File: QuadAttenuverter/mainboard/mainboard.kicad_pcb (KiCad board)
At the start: 2 copper layers, 35.6 x 108 mm, 48 parts, among them J1 Conn_01x09, J2 Conn_02x10_Counter_Clockwise, J3 Conn_02x05_Odd_Even, U1 LM324, U2 LM324, U3 LM324, U4 LM324, U5 LM324

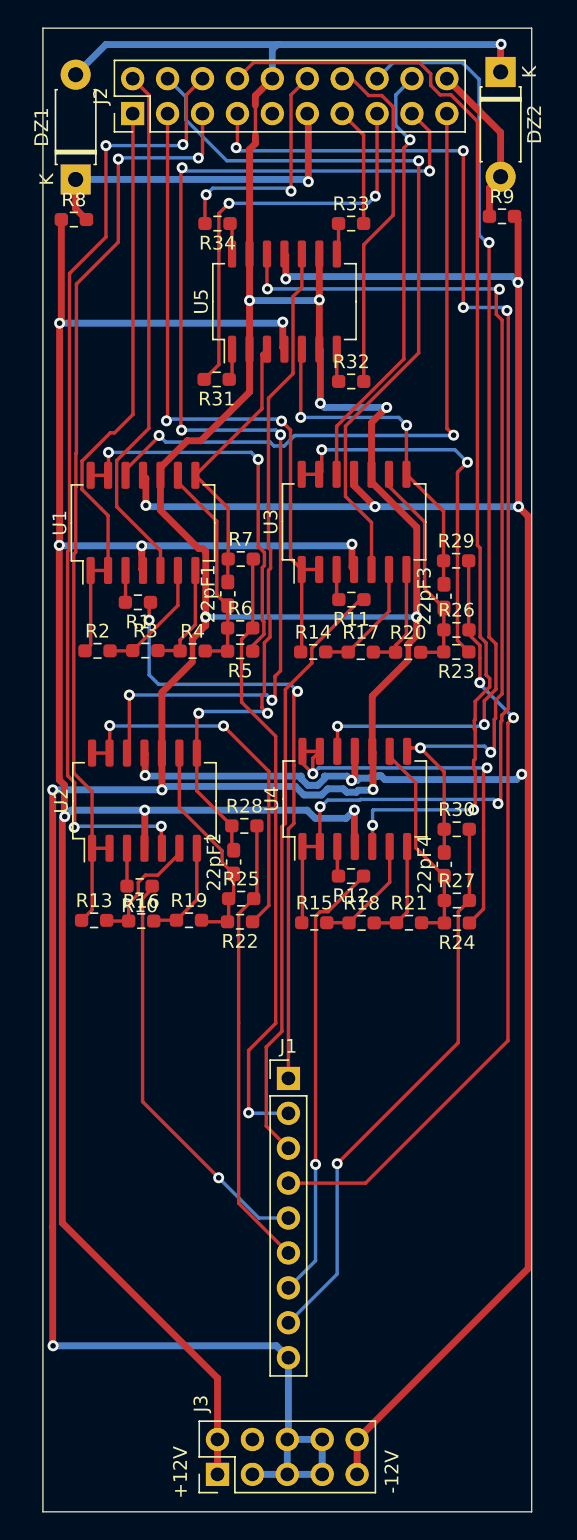
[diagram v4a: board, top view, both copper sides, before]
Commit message: Add IOBoard with the right knob distance
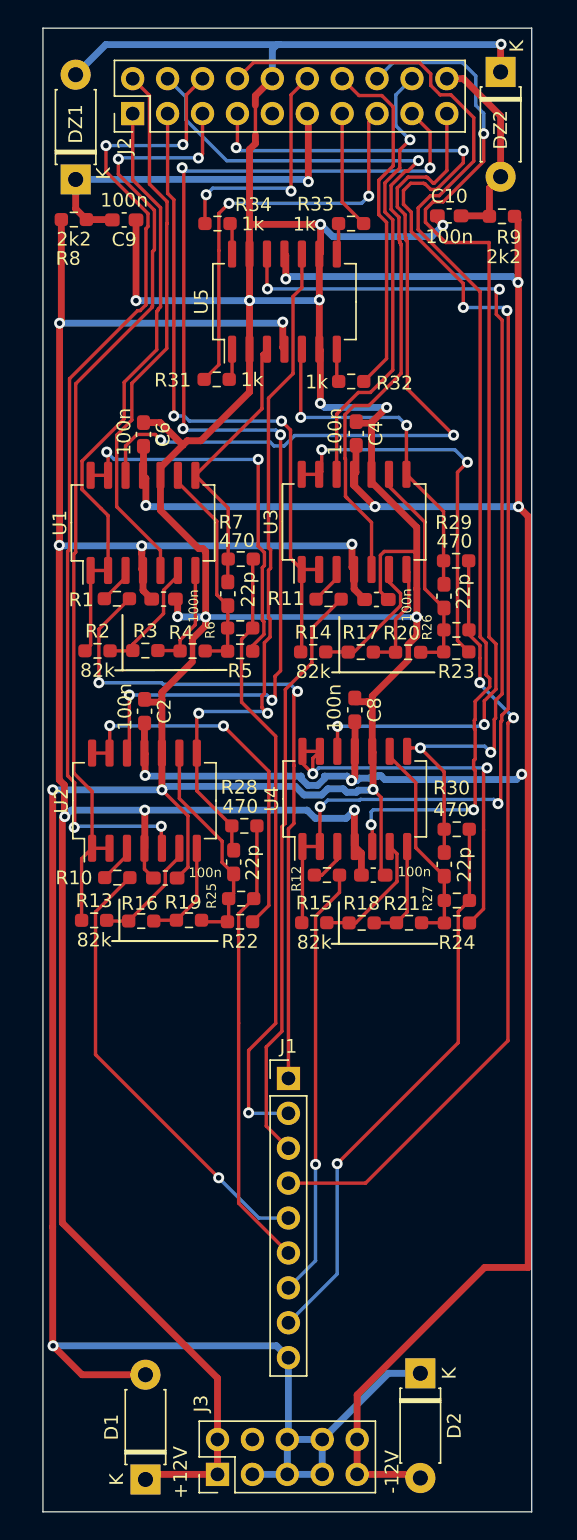
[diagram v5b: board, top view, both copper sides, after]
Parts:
- added C1: 100n, Capacitor_SMD:C_0603_1608Metric_Pad1.08x0.95mm_HandSolder, F.Cu at (107.4, 80.9)
- added C10: 100n, Capacitor_SMD:C_0603_1608Metric_Pad1.08x0.95mm_HandSolder, F.Cu at (112.7, 53.0)
- added C2: 100n, Capacitor_SMD:C_0603_1608Metric_Pad1.08x0.95mm_HandSolder, F.Cu at (90.5, 89.1)
- added C3: 100n, Capacitor_SMD:C_0603_1608Metric_Pad1.08x0.95mm_HandSolder, F.Cu at (107.2, 101.0)
- added C4: 100n, Capacitor_SMD:C_0603_1608Metric_Pad1.08x0.95mm_HandSolder, F.Cu at (105.9, 68.8)
- added C5: 100n, Capacitor_SMD:C_0603_1608Metric_Pad1.08x0.95mm_HandSolder, F.Cu at (91.9, 80.9)
- added C6: 100n, Capacitor_SMD:C_0603_1608Metric_Pad1.08x0.95mm_HandSolder, F.Cu at (90.5, 68.9)
- added C7: 100n, Capacitor_SMD:C_0603_1608Metric_Pad1.08x0.95mm_HandSolder, F.Cu at (92.0, 101.2)
- added C8: 100n, Capacitor_SMD:C_0603_1608Metric_Pad1.08x0.95mm_HandSolder, F.Cu at (105.8, 89.0)
- added C9: 100n, Capacitor_SMD:C_0603_1608Metric_Pad1.08x0.95mm_HandSolder, F.Cu at (89.0, 53.3)
- added D1: 1N4007, Diode_THT:D_DO-41_SOD81_P7.62mm_Horizontal, F.Cu at (90.6, 144.9)
- added D2: 1N4007, Diode_THT:D_DO-41_SOD81_P7.62mm_Horizontal, F.Cu at (110.6, 137.2)
- moved R12 1.75 mm to (103.8, 101.0)
- moved R10 1.73 mm to (88.5, 101.2)
- moved R11 1.66 mm to (103.9, 80.9)
- moved R1 1.55 mm to (88.5, 80.9)
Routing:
- net GND: track 263.2 -> 343.2 mm, vias 11 -> 15
- net +12V: track 167.4 -> 182.4 mm
- net -12V: track 181.1 -> 195.8 mm
- net /OFFSET4: track 68.9 -> 74.6 mm
- net /OFFSET1: track 49.7 -> 55.4 mm
- net /GAIN4IN: track 93.1 -> 98.4 mm
- net /IN1: track 45.1 -> 50.2 mm
- net /GAIN4OUT: track 81.3 -> 85.1 mm
- net /IN3: track 30.1 -> 32.9 mm
- net -5V: track 12.0 -> 14.8 mm
- net /GAIN3OUT: track 70.0 -> 72.6 mm
- net /GAIN3IN: track 68.1 -> 70.3 mm
- net +5V: track 25.2 -> 27.1 mm
- net /GAIN2OUT: track 54.4 -> 56.0 mm
- net /GAIN1IN: track 43.0 -> 44.5 mm
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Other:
- board text added: "22p"

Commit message: Few faceplate cleanups to get rid of warnings
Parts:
- C11: renamed from 22pF2; value C -> 22pF
- C12: renamed from 22pF1; value C -> 22pF
- C13: renamed from 22pF3; value C -> 22pF
- C14: renamed from 22pF4; value C -> 22pF

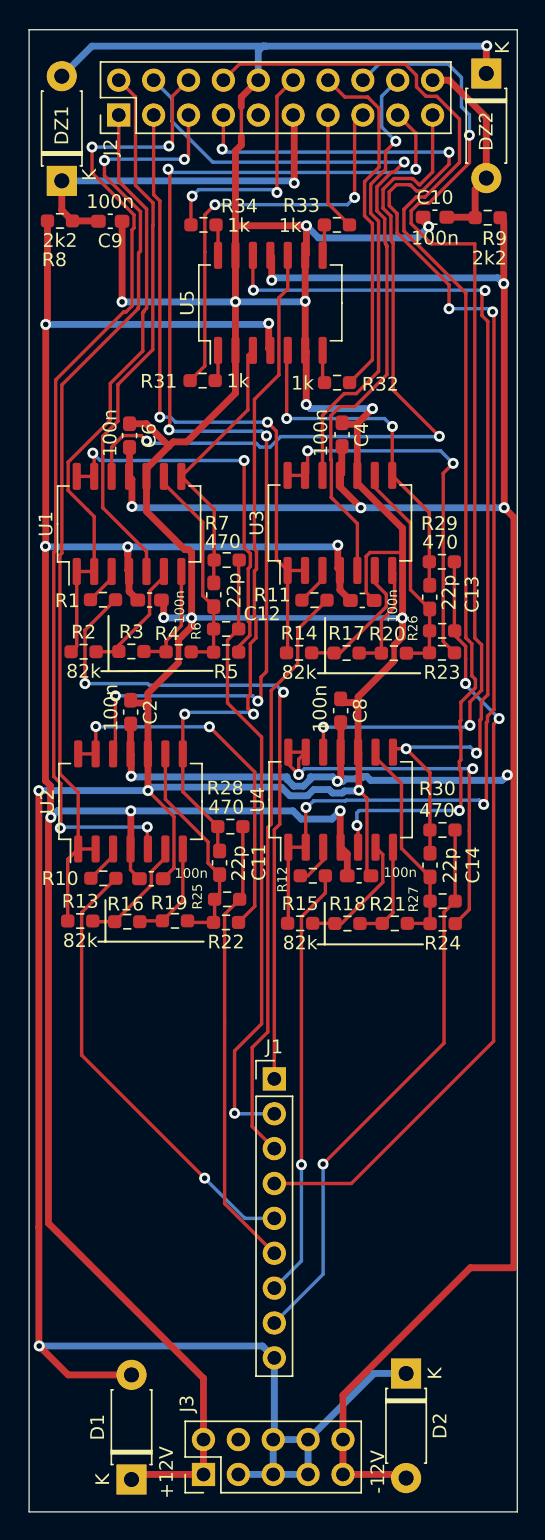
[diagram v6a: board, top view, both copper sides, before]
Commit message: Add electrolytic caps and inrush resistors
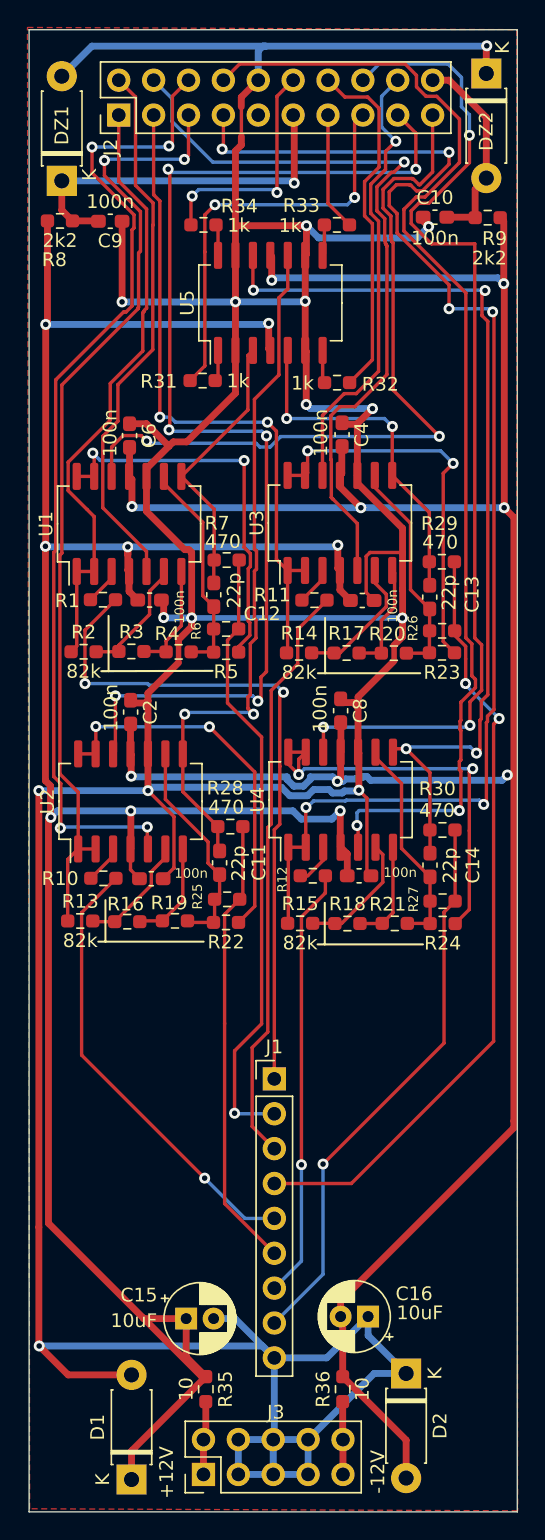
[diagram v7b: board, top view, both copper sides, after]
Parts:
- added C15: 10uF, Capacitor_THT:CP_Radial_D5.0mm_P2.00mm, F.Cu at (94.6, 133.2)
- added C16: 10uF, Capacitor_THT:CP_Radial_D5.0mm_P2.00mm, F.Cu at (107.8, 133.1)
- added R35: 10, Resistor_SMD:R_0603_1608Metric_Pad0.98x0.95mm_HandSolder, F.Cu at (96.0, 138.4)
- added R36: 10, Resistor_SMD:R_0603_1608Metric_Pad0.98x0.95mm_HandSolder, F.Cu at (106.0, 138.4)
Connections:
- J3 pad 1: +12V -> Net-(J3-Pad1)
- J3 pad 10: -12V -> Net-(J3-Pad10)
- J3 pad 2: +12V -> Net-(J3-Pad1)
- J3 pad 4: unconnected-(J3-Pad4) -> GND
- J3 pad 9: -12V -> Net-(J3-Pad10)
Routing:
- net GND: track 343.2 -> 367.2 mm
- net +12V: track 182.4 -> 187.8 mm
- net Net-(J3-Pad1): track 0.00 -> 5.37 mm
- net Net-(J3-Pad10): track 0.00 -> 5.31 mm
- net -12V: track 195.8 -> 191.5 mm
- added copper zone on F.Cu, net GND

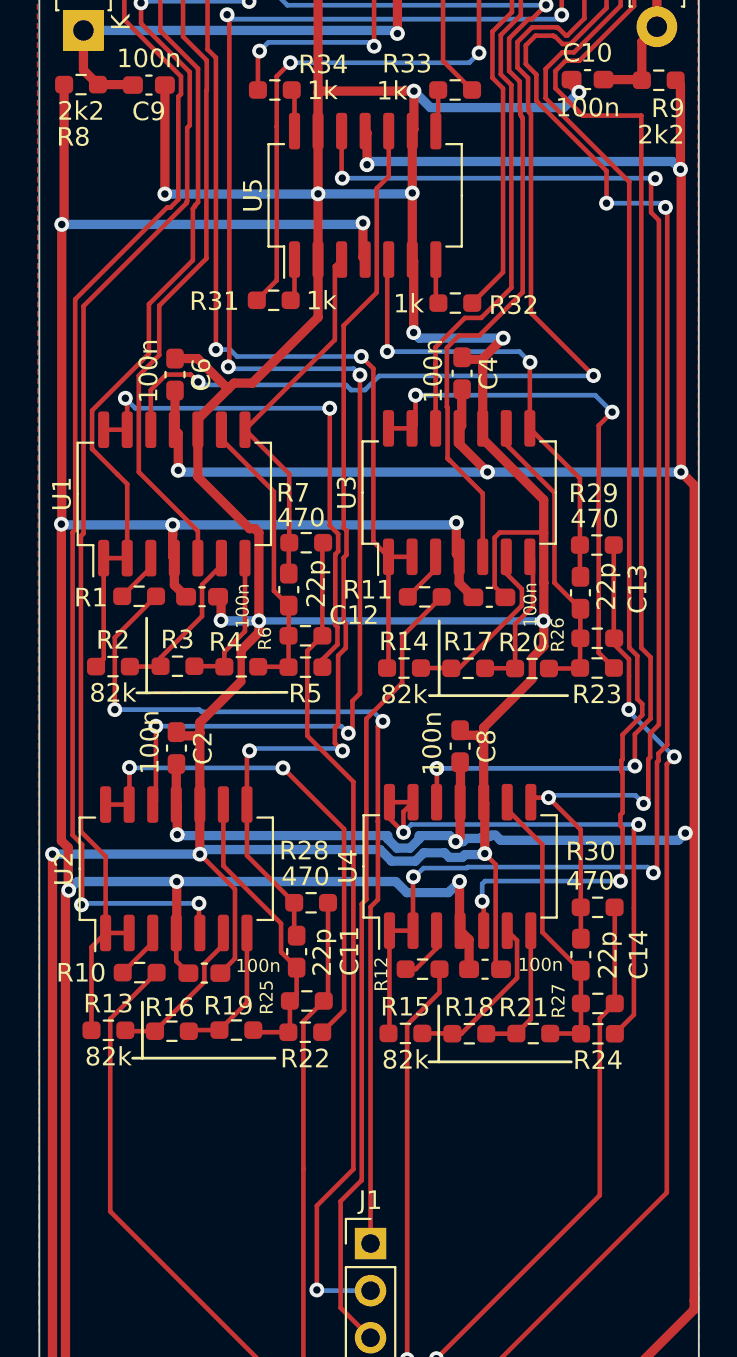
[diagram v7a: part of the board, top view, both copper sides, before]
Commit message: Adjusted LM324 to actual SO14 package
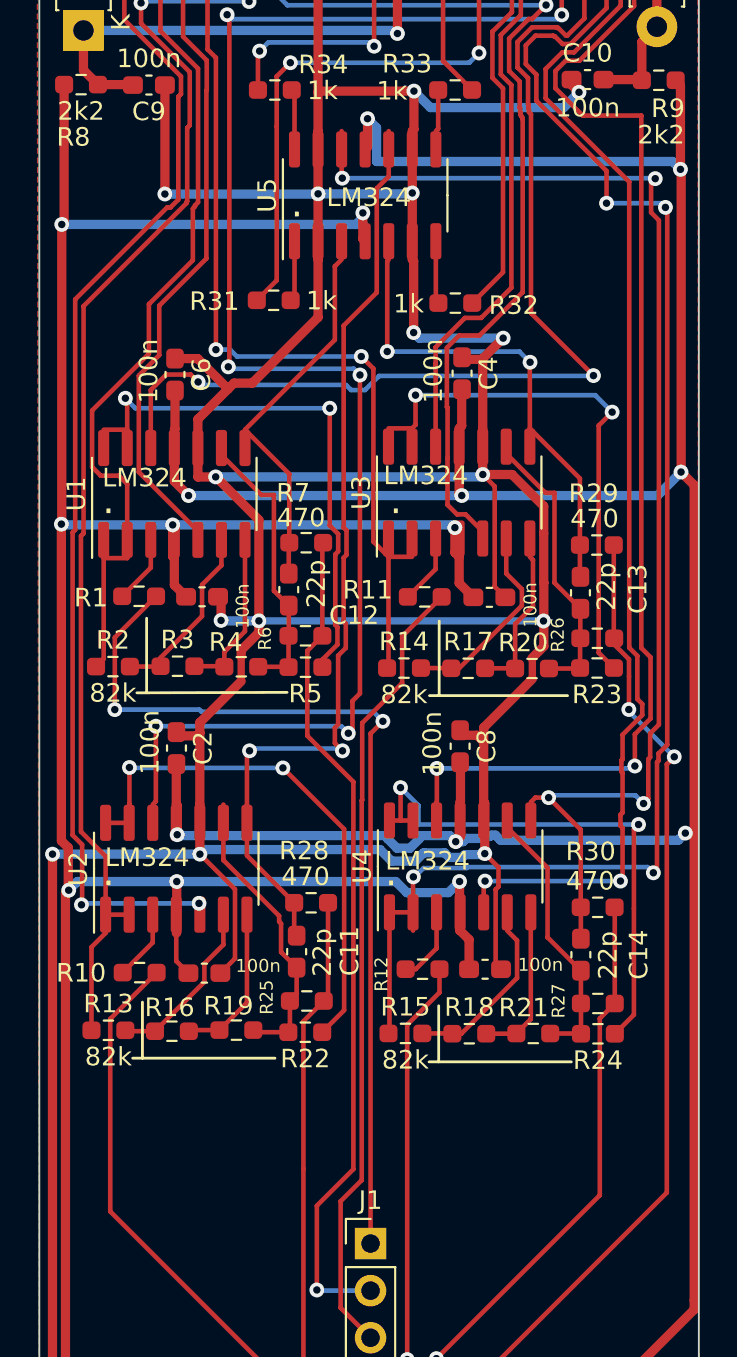
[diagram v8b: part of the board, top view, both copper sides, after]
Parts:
- U1, U2, U3, U4, U5: footprint Package_SO:SO-14_5.3x10.2mm_P1.27mm -> Package_SO:SO-14_3.9x8.65mm_P1.27mm
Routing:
- net GND: track 367.2 -> 383.6 mm, vias 15 -> 17
- net -12V: track 191.5 -> 194.4 mm
- net /GAIN3OUT: track 72.6 -> 71.0 mm
- net /GAIN1OUT: track 39.7 -> 38.2 mm
- net /GAIN4OUT: track 85.1 -> 84.0 mm
- net Net-(C14-Pad1): track 15.8 -> 14.8 mm
- net /GAIN2OUT: track 56.0 -> 55.1 mm
- net Net-(C13-Pad1): track 16.3 -> 15.6 mm
- net Net-(R24-Pad1): track 29.7 -> 29.1 mm
- net Net-(C12-Pad1): track 16.0 -> 15.4 mm
- net /GAIN1IN: track 44.5 -> 45.1 mm
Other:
- board text added: "."
